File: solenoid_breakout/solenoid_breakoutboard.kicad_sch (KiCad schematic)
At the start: 27 parts, among them J1 Conn_01x04_Pin, J2 Conn_01x04_Pin, J3 Conn_01x04_Pin, J4 Conn_01x04_Pin, J7 Conn_01x05, J8 Conn_01x05, Q2 AO3400A, Q5 AO3400A, Q6 AO3400A, Q7 AO3400A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

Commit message: small fixes
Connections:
- net +5V: now also D2.1 (K), D3.1 (K), D4.1 (K), L2.2, L3.2, L4.2
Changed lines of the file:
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@@
 	)
 	(symbol
+		(lib_id "power:+5V")
+		(at 201.93 125.73 0)
+		(unit 1)
+		(exclude_from_sim no)
+		(in_bom yes)
+		(on_board yes)
+		(dnp no)
+		(fields_autoplaced yes)
+		(property "Reference" "#PWR026"
+			(at 201.93 129.54 0)
+			(effects
+				(font
+					(size 1.27 1.27)
+				)
+				(hide yes)
+			)
+		)
+		(property "Value" "+5V"
+			(at 204.47 124.4599 0)
+			(effects
+				(font
+					(size 1.27 1.27)
+				)
+				(justify left)
+			)
+		)
+		(property "Footprint" ""
+			(at 201.93 125.73 0)
+			(effects
+				(font
+					(size 1.27 1.27)
+				)
+				(hide yes)
+			)
+		)
+		(property "Datasheet" ""
+			(at 201.93 125.73 0)
+			(effects
+				(font
+					(size 1.27 1.27)
+				)
+				(hide yes)
+			)
+		)
+		(property "Description" "Power symbol creates a global label with name \"+5V\""
+			(at 201.93 125.73 0)
+			(effects
+				(font
+					(size 1.27 1.27)
+				)
+				(hide yes)
+			)
+		)
+		(pin "1"
+		)
+		(instances
+			(project "solenoid_breakoutboard"
+				(path "/ee838435-3068-41d2-af0e-f8fb497bce61"
+					(reference "#PWR026")
+					(unit 1)
+				)
+			)
+		)
+	)
+	(symbol
 		(lib_id "Transistor_FET:AO3400A")
 		(at 185.42 123.19 0)
@@
 	)
 	(symbol
+		(lib_id "power:+5V")
+		(at 194.31 97.79 0)
+		(unit 1)
+		(exclude_from_sim no)
+		(in_bom yes)
+		(on_board yes)
+		(dnp no)
+		(fields_autoplaced yes)
+		(property "Reference" "#PWR025"
+			(at 194.31 101.6 0)
+			(effects
+				(font
+					(size 1.27 1.27)
+				)
+				(hide yes)
+			)
+		)
+		(property "Value" "+5V"
+			(at 196.85 96.5199 0)
+			(effects
+				(font
+					(size 1.27 1.27)
+				)
+				(justify left)
+			)
+		)
+		(property "Footprint" ""
+			(at 194.31 97.79 0)
+			(effects
+				(font
+					(size 1.27 1.27)
+				)
+				(hide yes)
+			)
+		)
+		(property "Datasheet" ""
+			(at 194.31 97.79 0)
+			(effects
+				(font
+					(size 1.27 1.27)
+				)
+				(hide yes)
+			)
+		)
+		(property "Description" "Power symbol creates a global label with name \"+5V\""
+			(at 194.31 97.79 0)
+			(effects
+				(font
+					(size 1.27 1.27)
+				)
+				(hide yes)
+			)
+		)
+		(pin "1"
+		)
+		(instances
+			(project "solenoid_breakoutboard"
+				(path "/ee838435-3068-41d2-af0e-f8fb497bce61"
+					(reference "#PWR025")
+					(unit 1)
+				)
+			)
+		)
+	)
+	(symbol
 		(lib_id "power:+3.3V")
 		(at 35.56 158.75 90)
@@
 					(unit 1)
 				)
+			)
+		)
+	)
+	(symbol
+		(lib_id "power:+5V")
+		(at 189.23 57.15 0)
+		(unit 1)
+		(exclude_from_sim no)
+		(in_bom yes)
+		(on_board yes)
+		(dnp no)
+		(fields_autoplaced yes)
+		(property "Reference" "#PWR024"
+			(at 189.23 60.96 0)
+			(effects
+				(font
+					(size 1.27 1.27)
+				)
+				(hide yes)
+			)
+		)
+		(property "Value" "+5V"
+			(at 191.77 55.8799 0)
+			(effects
+				(font
+					(size 1.27 1.27)
+				)
+				(justify left)
+			)
+		)
+		(property "Footprint" ""
+			(at 189.23 57.15 0)
+			(effects
+				(font
+					(size 1.27 1.27)
+				)
+				(hide yes)
+			)
+		)
+		(property "Datasheet" ""
+			(at 189.23 57.15 0)
+			(effects
+				(font
+					(size 1.27 1.27)
+				)
+				(hide yes)
+			)
+		)
+		(property "Description" "Power symbol creates a global label with name \"+5V\""
+			(at 189.23 57.15 0)
+			(effects
+				(font
+					(size 1.27 1.27)
+				)
+				(hide yes)
+			)
+		)
+		(pin "1"
+		)
+		(instances
+			(project "solenoid_breakoutboard"
+				(path "/ee838435-3068-41d2-af0e-f8fb497bce61"
+					(reference "#PWR024")
+					(unit 1)
+				)

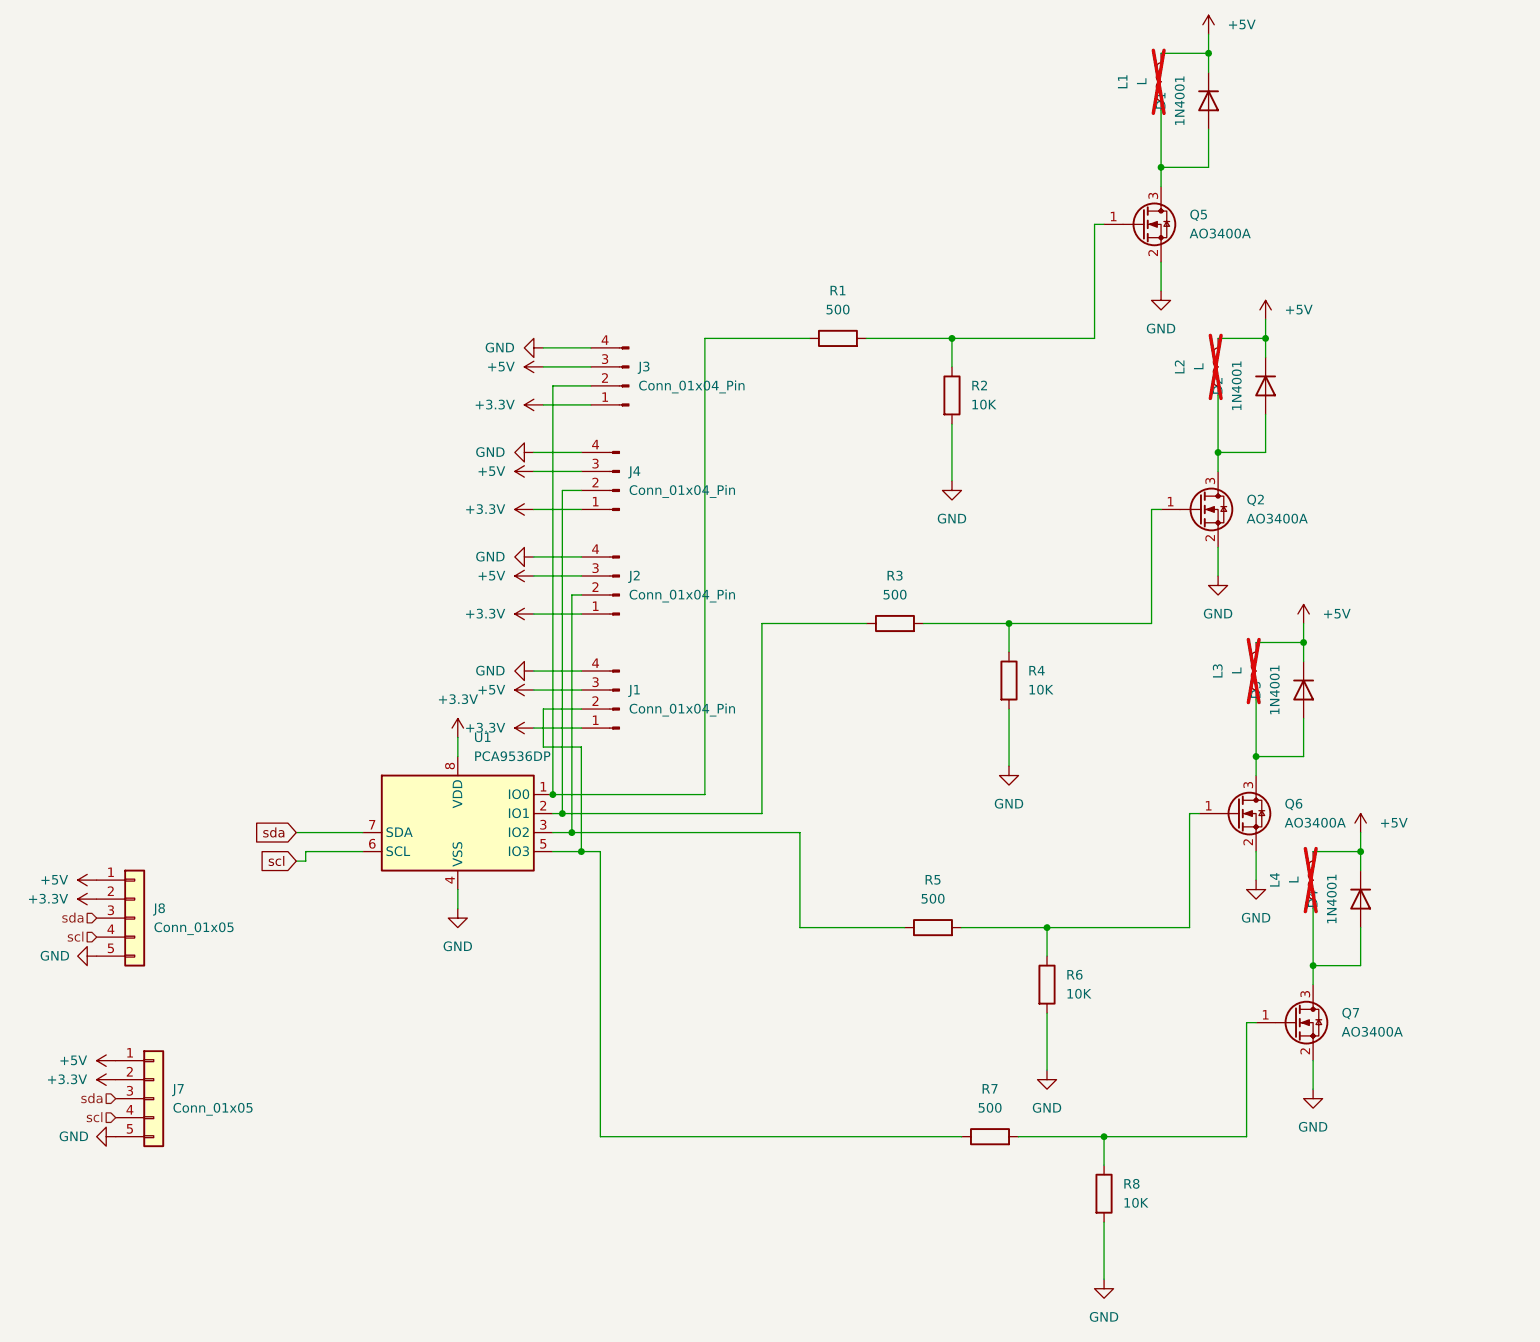
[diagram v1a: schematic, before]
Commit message: added onboarding and fixed pcb models
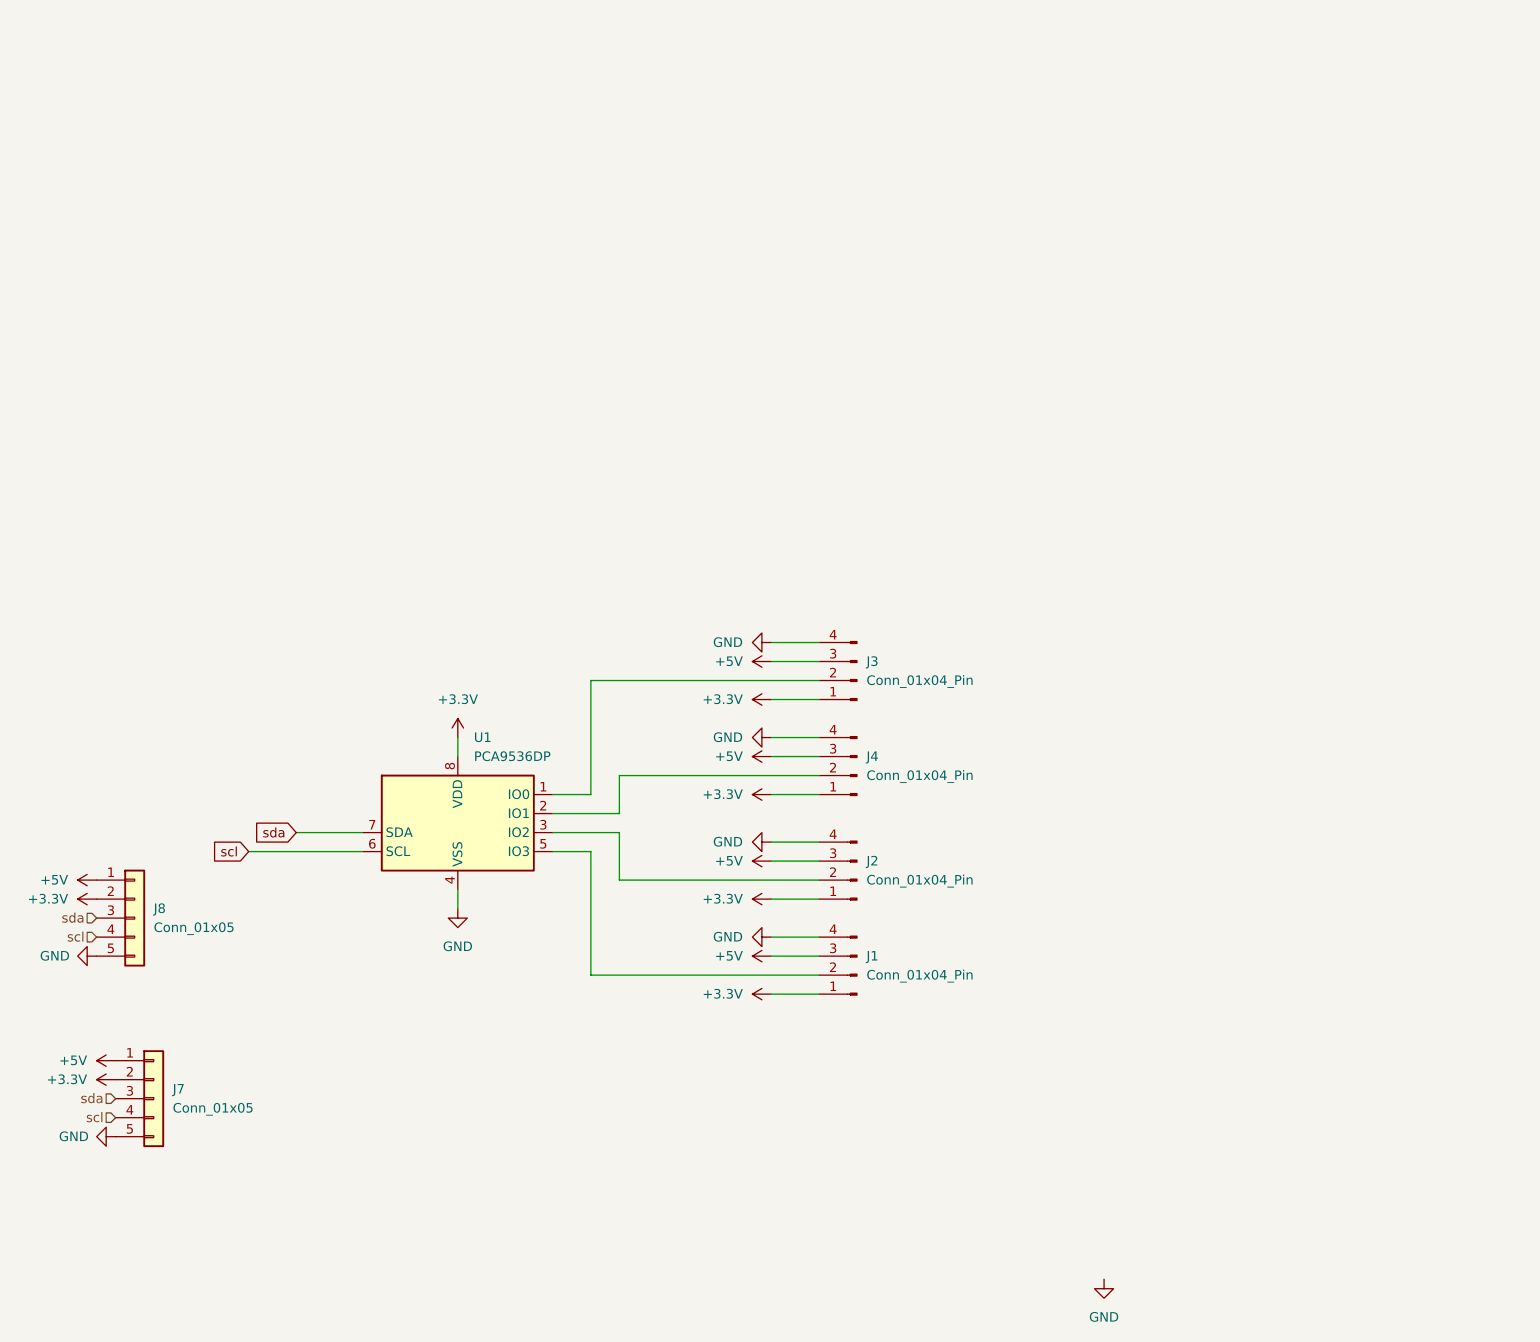
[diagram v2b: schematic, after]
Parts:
- removed D1, D2, D3, D4: 1N4001, Diode_SMD:D_SOD-123F, symbol Diode:1N4001
- removed L1, L2, L3, L4: L, Connector_PinHeader_2.54mm:PinHeader_1x02_P2.54mm_Vertical, symbol Device:L
- removed Q2, Q5, Q6, Q7: AO3400A, Package_TO_SOT_SMD:SOT-23, symbol Transistor_FET:AO3400A
- removed R1, R3, R5, R7: 500, Resistor_SMD:R_0603_1608Metric_Pad0.98x0.95mm_HandSolder, symbol Device:R
- removed R2, R4, R6, R8: 10K, Resistor_SMD:R_0603_1608Metric_Pad0.98x0.95mm_HandSolder, symbol Device:R
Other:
- moved on the sheet: J1, J2, J3, J4

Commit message: gpio board iteration 2 updated
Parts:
- added C1: 0.1uF, Capacitor_SMD:C_0402_1005Metric_Pad0.74x0.62mm_HandSolder, symbol Device:C_Small
- added J5, J6: Conn_01x10, pcb_footprints:GT-B0502MSV27-10S1101, symbol Connector_Generic:Conn_01x10
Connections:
- net +3.3V: now also C1.1, J5.9 (Pin_9), J6.9 (Pin_9)
- net +5V: now also J5.10 (Pin_10), J6.10 (Pin_10)
- net GND: now also C1.2, J5.6 (Pin_6), J6.6 (Pin_6)
- net scl: now also J5.7 (Pin_7), J6.7 (Pin_7)
- net sda: now also J5.8 (Pin_8), J6.8 (Pin_8)
- no-connect marks 0 -> 10

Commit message: gpio iteration 2 update
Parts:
- added C2, C3: 10uF, Capacitor_SMD:C_0402_1005Metric_Pad0.74x0.62mm_HandSolder, symbol Device:C_Small
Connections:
- net +3.3V: now also C2.1, C3.1
- net GND: now also C2.2, C3.2

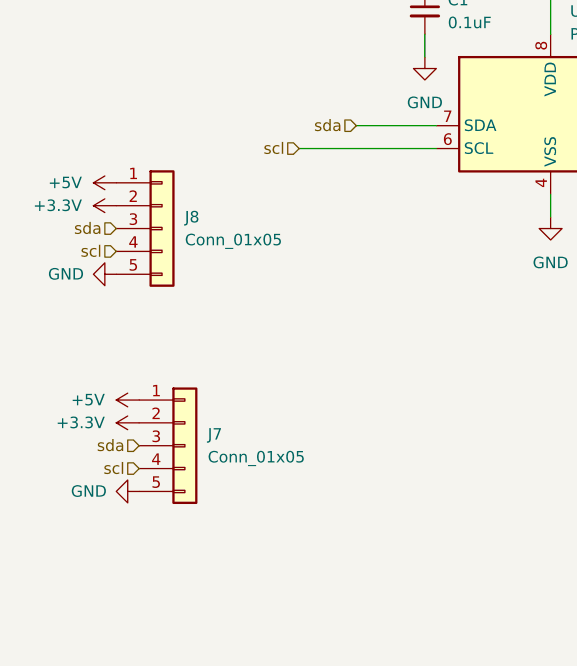
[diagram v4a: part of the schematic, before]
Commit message: finished base board PCB + created production files for base board and modules
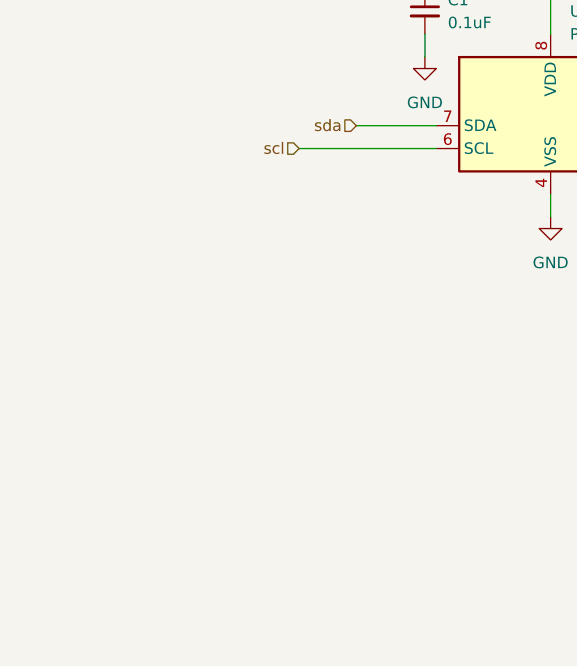
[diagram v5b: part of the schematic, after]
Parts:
- removed J7, J8: Conn_01x05, Connector_PinHeader_2.54mm:PinHeader_1x05_P2.54mm_Vertical, symbol Connector_Generic:Conn_01x05
- C1: Manufacturer Name (none) -> Samsung Electro-Mechanics; Manufacturer Part Number (none) -> CL05B104KB54PNC
- C2, C3: Manufacturer Name (none) -> Samsung Electro-Mechanics; Manufacturer Part Number (none) -> CL10A106KP8NNNC
- J1, J2, J3, J4: now left out of the parts list
- J5, J6: Manufacturer Name (none) -> G-Switch; Manufacturer Part Number (none) -> GT-B0502MSV27-10S1101
- U1: Manufacturer Name (none) -> Texas Instruments; Manufacturer Part Number (none) -> TCA9536DTMR

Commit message: updated production files
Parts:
- U1: value PCA9536DP -> TCA9536DTMR
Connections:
- net +3.3V: now also J5.7 (Pin_7), J6.7 (Pin_7); no longer J5.9 (Pin_9), J6.9 (Pin_9)
- net +5V: now also J5.6 (Pin_6), J6.6 (Pin_6); no longer J5.10 (Pin_10), J6.10 (Pin_10)
- net GND: now also J5.10 (Pin_10), J6.10 (Pin_10); no longer J5.6 (Pin_6), J6.6 (Pin_6)
- net scl: now also J5.9 (Pin_9), J6.9 (Pin_9); no longer J5.7 (Pin_7), J6.7 (Pin_7)
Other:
- moved on the sheet: C2, C3
